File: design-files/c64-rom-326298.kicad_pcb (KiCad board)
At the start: 2 copper layers, 76.2 x 33 mm, 14 parts, among them J1 Conn_01x12_Pin, J2 Conn_01x12_Pin, J3 Conn_01x02_Pin, J4 Conn_01x04_Pin, J5 Conn_01x12_Pin, SW101 SW_DIP_x02, SW102 SW_DIP_x02, SW103 SW_DIP_x02, U101 SST39SF010, U102 GAL22V10

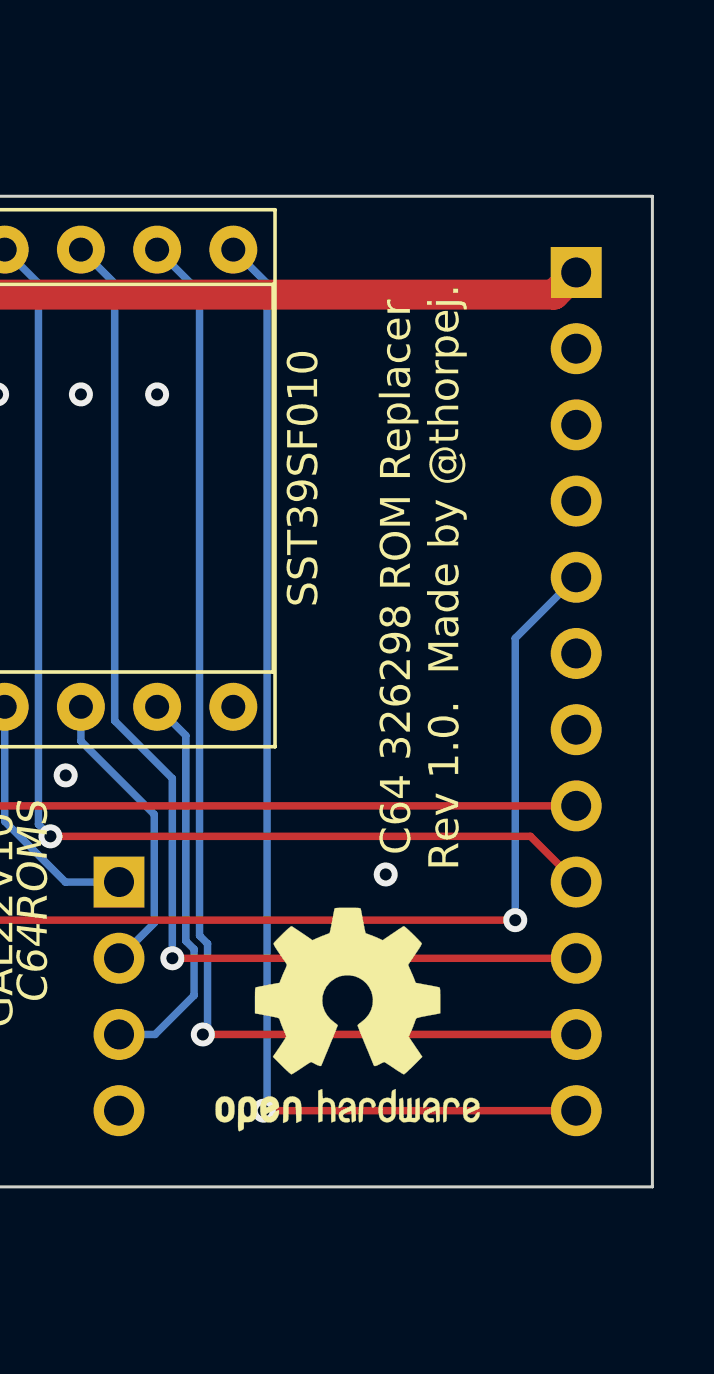
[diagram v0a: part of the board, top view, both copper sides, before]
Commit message: Add URL to the board.
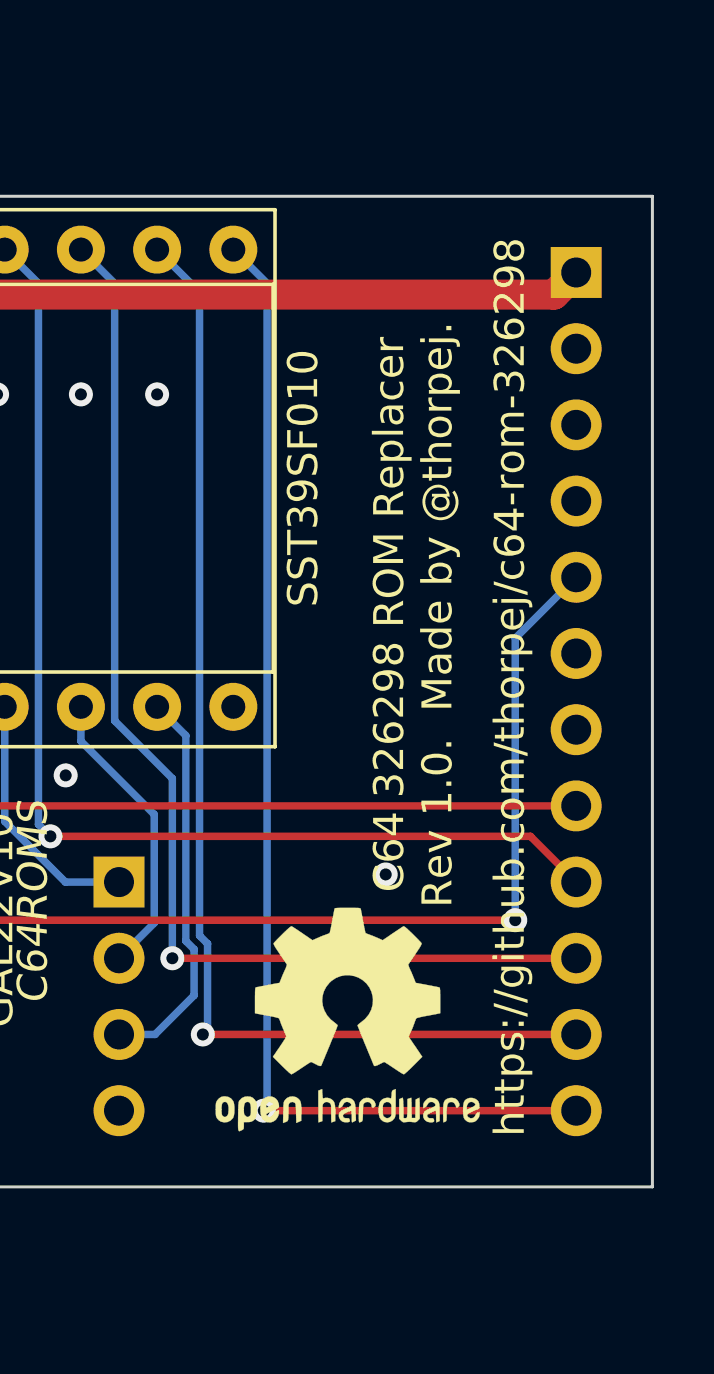
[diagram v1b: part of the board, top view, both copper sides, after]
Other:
- board text added: "https://github.com/thorpej/c64-rom-326298"

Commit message: More ground plane action.
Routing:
- net D6: track 38.3 -> 39.3 mm
- net D2: track 13.2 -> 12.5 mm

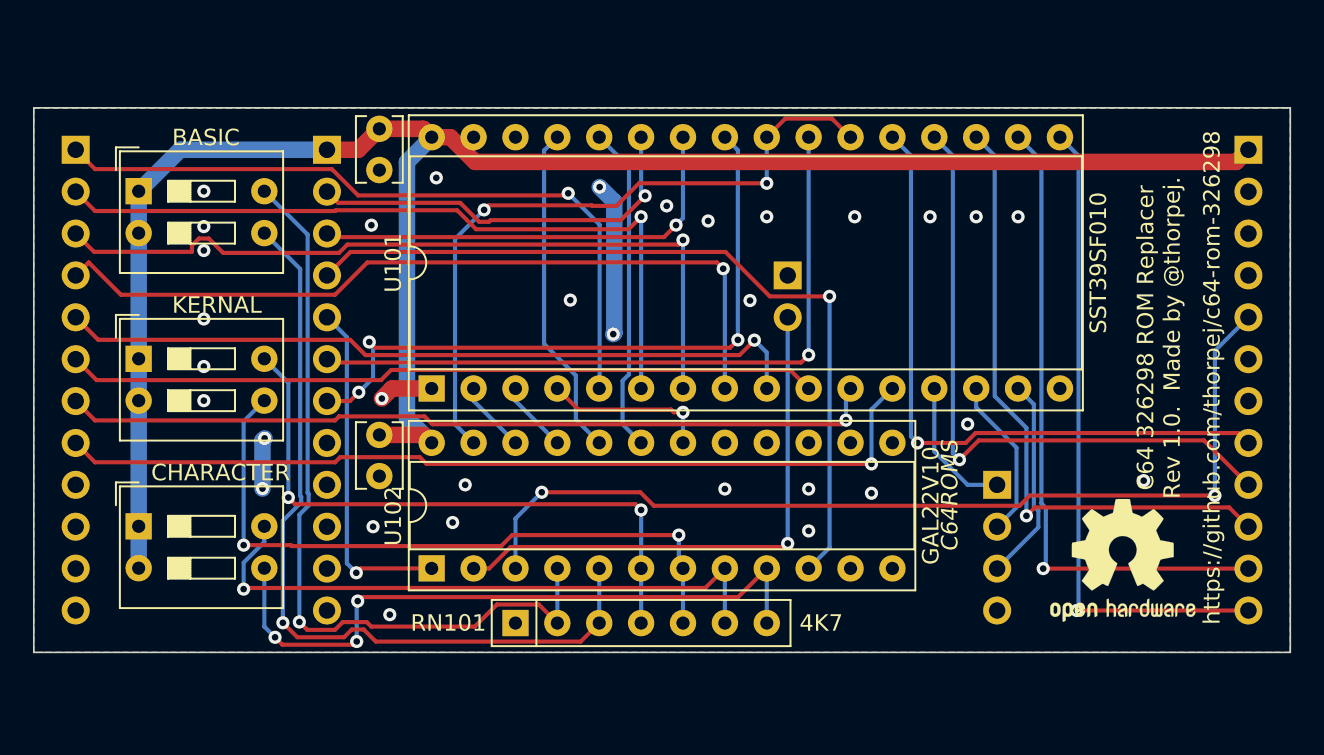
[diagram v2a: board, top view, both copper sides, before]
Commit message: Re-arrange the inputs to the GAL and make them active-low.
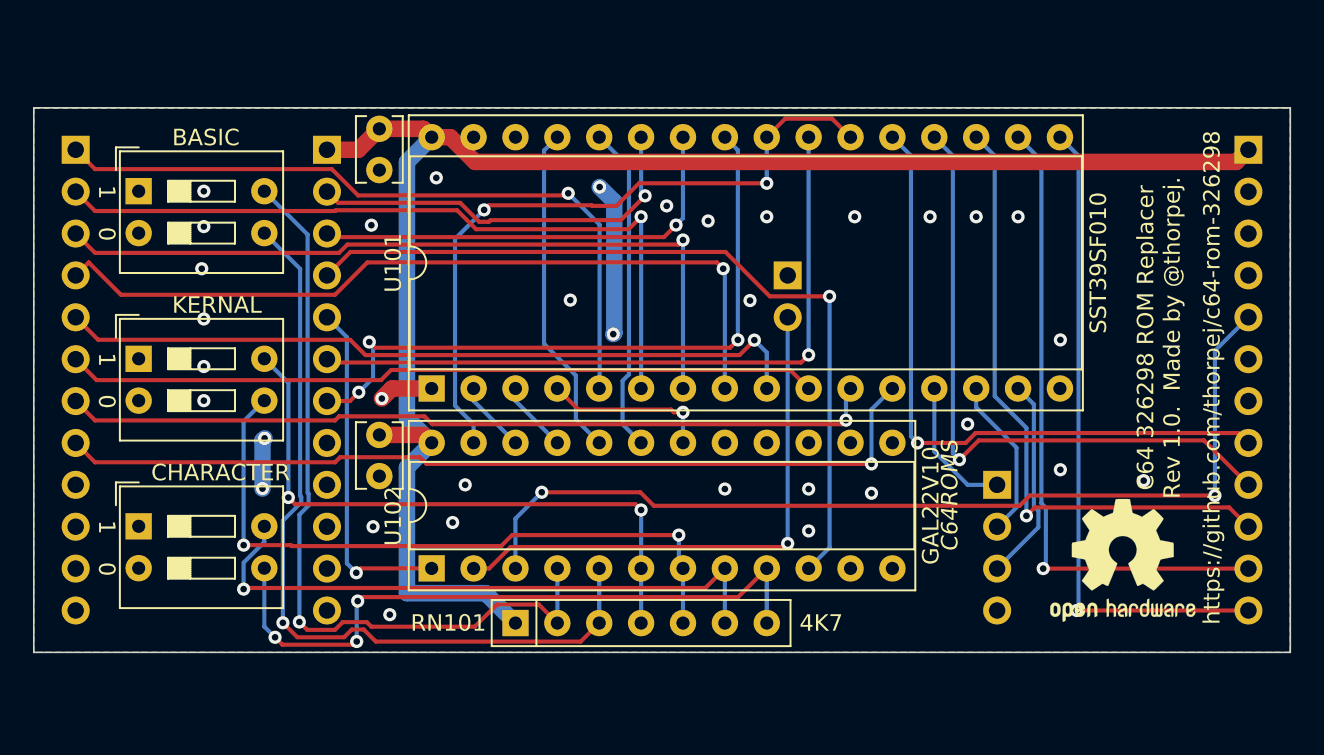
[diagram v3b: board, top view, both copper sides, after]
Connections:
- RN101 pad 1: VSS -> VCC
- SW101 pad 1: VCC -> VSS
- SW101 pad 2: VCC -> VSS
- SW102 pad 1: VCC -> VSS
- SW102 pad 2: VCC -> VSS
- SW103 pad 1: VCC -> VSS
- SW103 pad 2: VCC -> VSS
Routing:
- net VCC: track 116.0 -> 97.8 mm
- net A5: track 47.5 -> 46.6 mm
- net VSS: vias 32 -> 34
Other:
- board text added: "0"
- board text added: "1"

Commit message: Correct ROM socket pin header spacing.
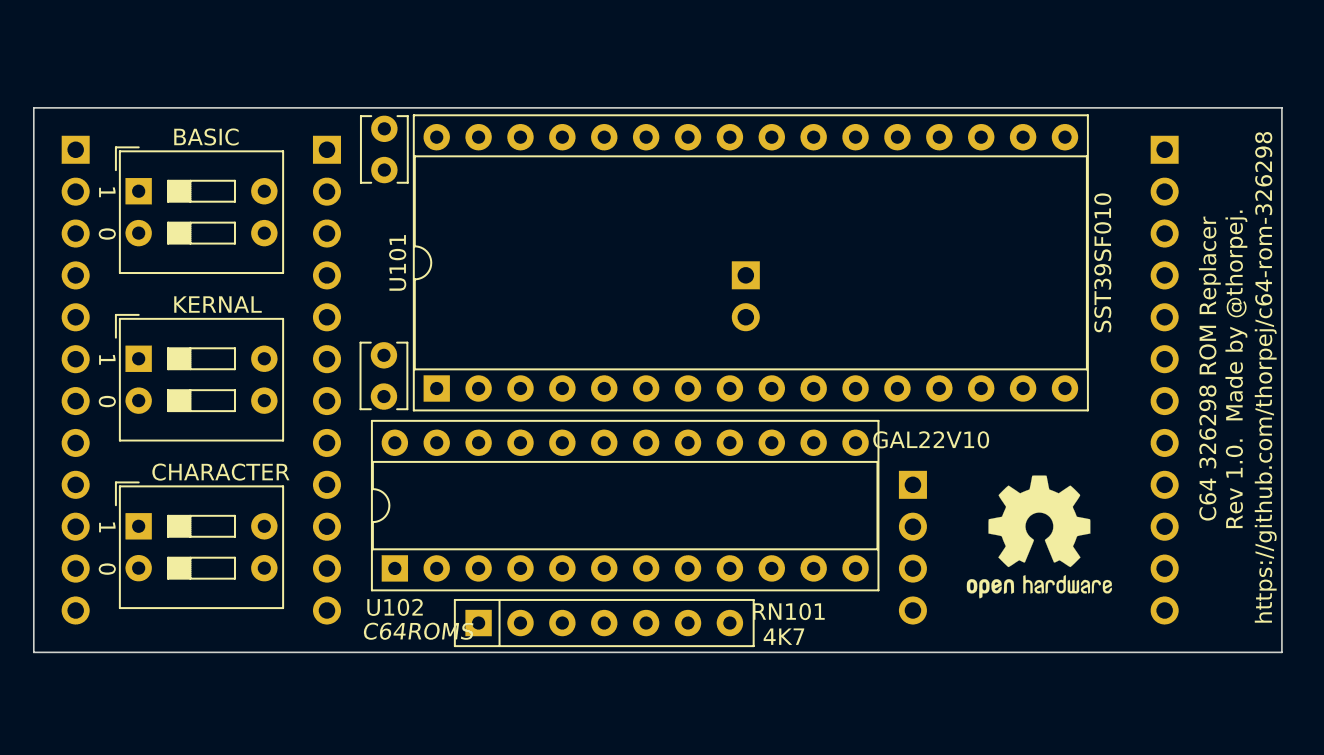
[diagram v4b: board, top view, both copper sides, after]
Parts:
- moved REF** 5.25 mm to (172.5, 109.0)
- moved J4 5.11 mm to (164.8, 105.8)
- moved J5 5.08 mm to (180.1, 85.5)
- moved J3 2.54 mm to (154.7, 93.1)
- moved C102 2.34 mm to (132.7, 100.5), turned to 90 degrees
- moved RN101 2.24 mm to (138.5, 114.2)
- moved U102 2.24 mm to (133.4, 110.9)
- moved C101 0.30 mm to (132.7, 84.2)
- moved U101 0.30 mm to (135.9, 100.0)
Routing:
- net VCC: track 97.8 -> 0.00 mm
- net ~{CHR}: track 58.3 -> 0.00 mm, vias 2 -> 0
- net A0: track 54.1 -> 0.00 mm, vias 1 -> 0
- net A1: track 49.6 -> 0.00 mm, vias 1 -> 0
- net IA12: track 49.2 -> 0.00 mm, vias 1 -> 0
- net Net-(RN101-R2): track 48.8 -> 0.00 mm, vias 1 -> 0
- net A4: track 48.7 -> 0.00 mm, vias 1 -> 0
- net Net-(RN101-R1): track 48.0 -> 0.00 mm, vias 1 -> 0
- net A5: track 46.6 -> 0.00 mm, vias 1 -> 0
- net A6: track 46.0 -> 0.00 mm, vias 1 -> 0
- net A3: track 45.7 -> 0.00 mm, vias 1 -> 0
- net A2: track 45.7 -> 0.00 mm
- net A7: track 43.7 -> 0.00 mm, vias 1 -> 0
- net A10: track 42.7 -> 0.00 mm, vias 1 -> 0
- net Net-(U101-CE): track 42.0 -> 0.00 mm, vias 2 -> 0
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- removed copper zone on B.Cu, net VSS
- removed copper zone on F.Cu, net VSS
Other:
- board size 76.2 x 33 mm -> 75.7 x 33 mm

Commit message: Re-route the boards after fixing the pin spacing.
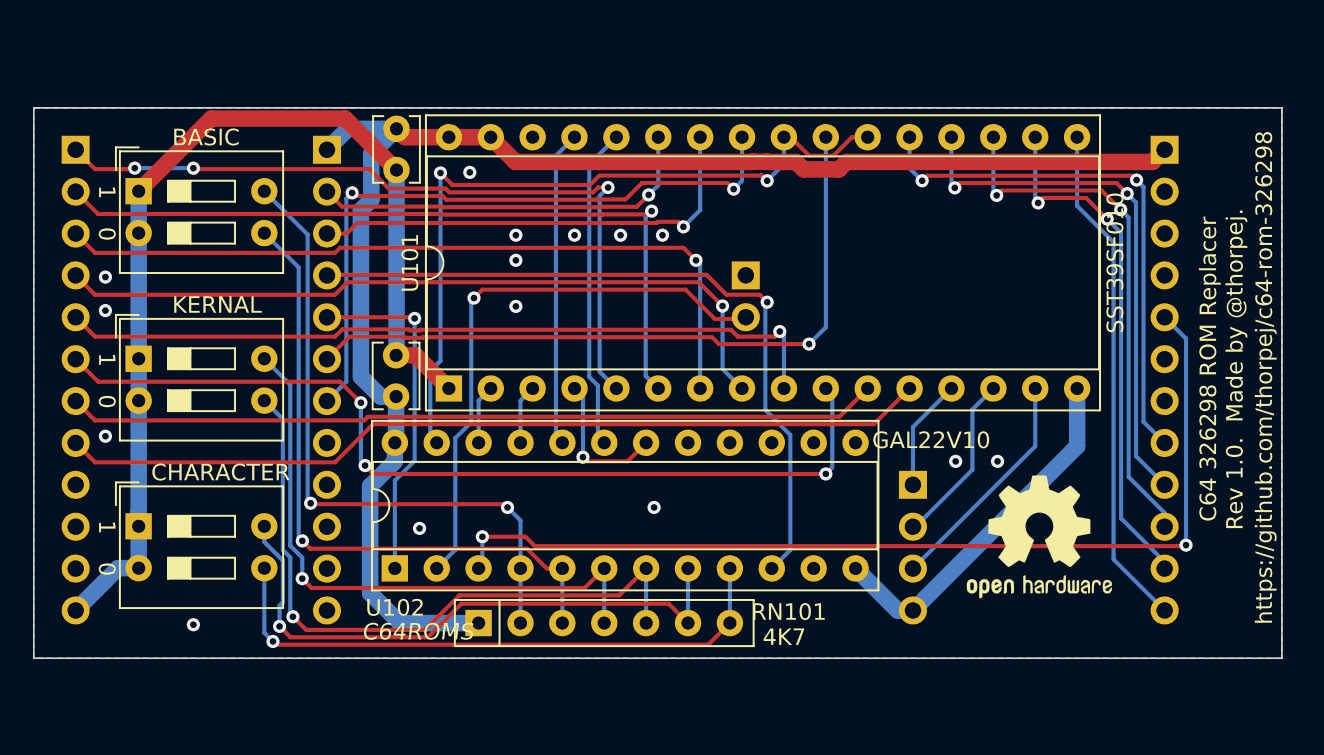
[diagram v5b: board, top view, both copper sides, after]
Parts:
- moved C101 0.74 mm to (133.5, 84.2)
- moved C102 0.74 mm to (133.5, 100.5)
- moved U101 0.74 mm to (136.7, 100.0)
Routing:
- net VCC: track 0.00 -> 91.3 mm
- net VSS: track 0.00 -> 84.8 mm, vias 0 -> 15
- net ~{CHR}: track 0.00 -> 59.3 mm, vias 0 -> 2
- net A2: track 0.00 -> 56.0 mm, vias 0 -> 3
- net A0: track 0.00 -> 52.9 mm
- net A1: track 0.00 -> 49.3 mm
- net A3: track 0.00 -> 47.3 mm, vias 0 -> 1
- net A6: track 0.00 -> 46.8 mm, vias 0 -> 1
- net A5: track 0.00 -> 46.4 mm, vias 0 -> 1
- net A7: track 0.00 -> 46.3 mm, vias 0 -> 3
- net Net-(U101-CE): track 0.00 -> 46.3 mm, vias 0 -> 2
- net A4: track 0.00 -> 46.1 mm, vias 0 -> 1
- net IA12: track 0.00 -> 44.7 mm, vias 0 -> 1
- net A10: track 0.00 -> 43.0 mm, vias 0 -> 1
- net A11: track 0.00 -> 40.5 mm, vias 0 -> 2
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- added copper zone on B.Cu, net VSS
- added copper zone on F.Cu, net VSS
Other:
- board size 75.7 x 33 mm -> 75.7 x 33.4 mm
